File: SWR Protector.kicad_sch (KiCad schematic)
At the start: 27 parts, among them J1 Barrel_Jack, J2 Barrel_Jack, J3 transceiver, J4 antenna, K2 ATX209, Q1 2N3904, T1 1:12, T2 1:12, U1 LM78L05_TO92, U2 LM358

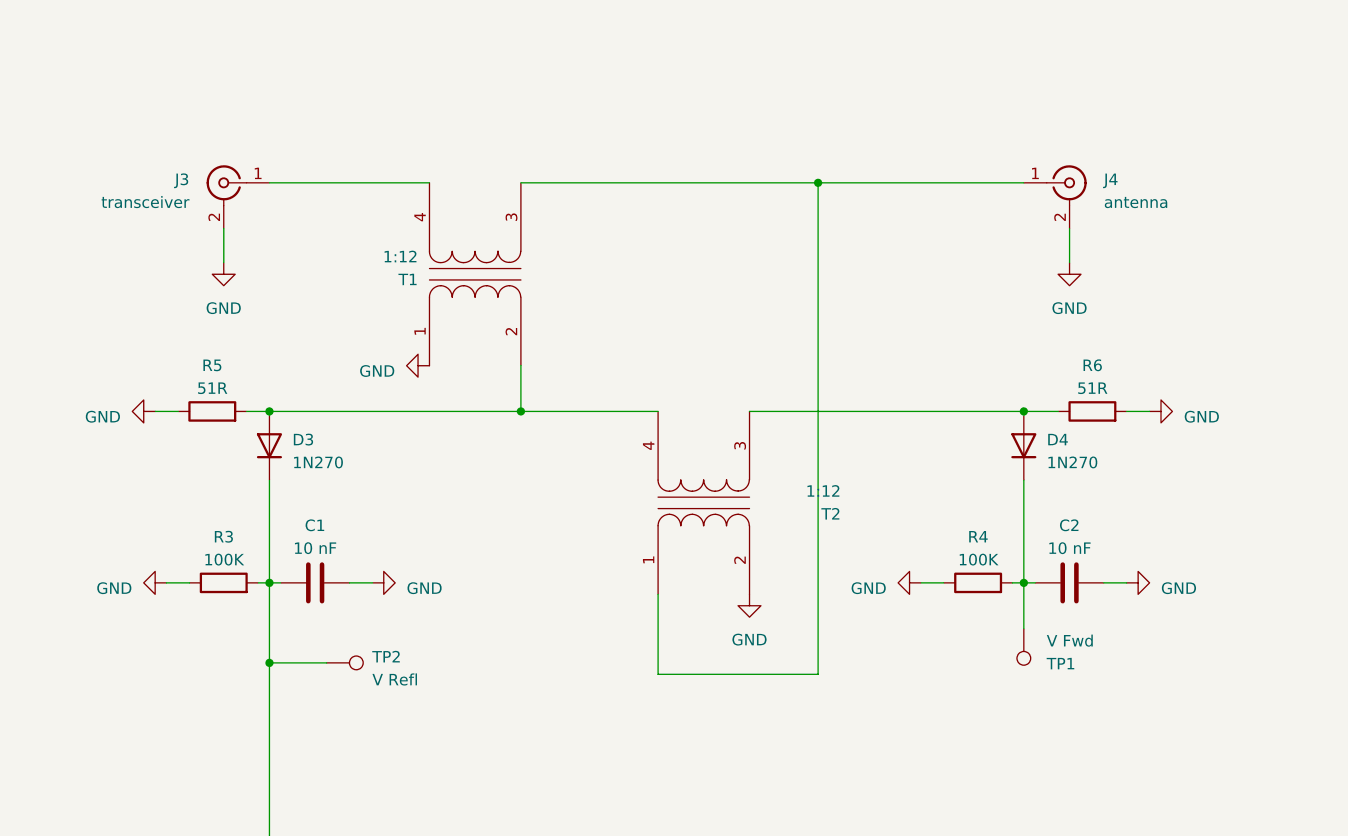
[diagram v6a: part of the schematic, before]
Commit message: moved transceiver BNC jack to the same side of the board as the switched pwr
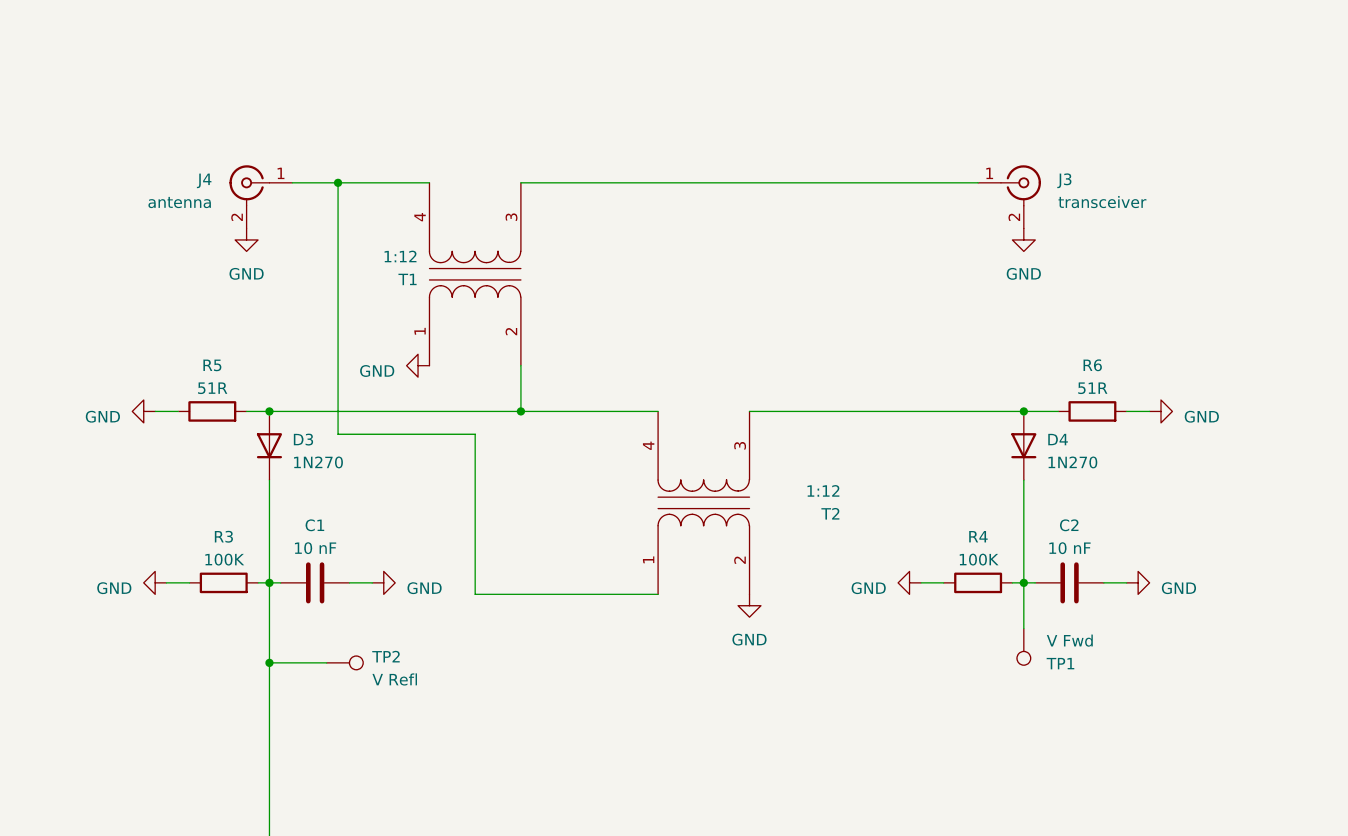
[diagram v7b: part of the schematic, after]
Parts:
- J1, J2: footprint Connector_BarrelJack:BarrelJack_Horizontal -> Connector_BarrelJack:BarrelJack_CUI_PJ-063AH_Horizontal
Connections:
- net at J4.1 (In), T2.1 (AA): now also T1.4 (SB); no longer T1.3 (SA)
- net at J3.1 (In): now also T1.3 (SA); no longer T1.4 (SB)
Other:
- moved on the sheet: J3, J4
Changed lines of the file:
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@@
     (rev "0.6")
   )
-  (junction (at 111.76 35.56) (diameter 0) (color 0 0 0 0)
-  )
   (junction (at 181.61 138.43) (diameter 0) (color 0 0 0 0)
   )
@@
   )
   (junction (at 134.62 60.96) (diameter 0) (color 0 0 0 0)
+  )
+  (junction (at 58.42 35.56) (diameter 0) (color 0 0 0 0)
   )
   (junction (at 240.03 29.21) (diameter 0) (color 0 0 0 0)
@@
     (stroke (width 0) (type default))
   )
+  (wire (pts (xy 58.42 63.5) (xy 58.42 35.56))
+    (stroke (width 0) (type default))
+  )
   (wire (pts (xy 134.62 80.01) (xy 135.89 80.01))
     (stroke (width 0) (type default))
@@
     (stroke (width 0) (type default))
   )
-  (wire (pts (xy 93.98 90.17) (xy 93.98 81.28))
+  (wire (pts (xy 73.66 63.5) (xy 58.42 63.5))
+    (stroke (width 0) (type default))
+  )
+  (wire (pts (xy 53.34 35.56) (xy 58.42 35.56))
     (stroke (width 0) (type default))
   )
@@
     (stroke (width 0) (type default))
   )
-  (wire (pts (xy 78.74 35.56) (xy 111.76 35.56))
-    (stroke (width 0) (type default))
-  )
   (wire (pts (xy 190.5 114.3) (xy 193.04 114.3))
     (stroke (width 0) (type default))
@@
     (stroke (width 0) (type default))
   )
-  (wire (pts (xy 111.76 90.17) (xy 93.98 90.17))
-    (stroke (width 0) (type default))
-  )
   (wire (pts (xy 50.8 60.96) (xy 78.74 60.96))
     (stroke (width 0) (type default))
   )
-  (wire (pts (xy 139.7 40.64) (xy 139.7 44.45))
+  (wire (pts (xy 58.42 35.56) (xy 68.58 35.56))
     (stroke (width 0) (type default))
   )
@@
     (stroke (width 0) (type default))
   )
-  (wire (pts (xy 45.72 40.64) (xy 45.72 44.45))
-    (stroke (width 0) (type default))
-  )
   (wire (pts (xy 181.61 138.43) (xy 181.61 143.51))
     (stroke (width 0) (type default))
@@
     (stroke (width 0) (type default))
   )
+  (wire (pts (xy 93.98 81.28) (xy 73.66 81.28))
+    (stroke (width 0) (type default))
+  )
   (wire (pts (xy 125.73 146.05) (xy 129.54 146.05))
     (stroke (width 0) (type default))
@@
     (stroke (width 0) (type default))
   )
-  (wire (pts (xy 111.76 35.56) (xy 111.76 90.17))
-    (stroke (width 0) (type default))
-  )
   (wire (pts (xy 168.91 138.43) (xy 181.61 138.43))
     (stroke (width 0) (type default))
   )
-  (wire (pts (xy 50.8 35.56) (xy 68.58 35.56))
-    (stroke (width 0) (type default))
-  )
   (wire (pts (xy 133.35 80.01) (xy 134.62 80.01))
     (stroke (width 0) (type default))
@@
     (stroke (width 0) (type default))
   )
+  (wire (pts (xy 73.66 81.28) (xy 73.66 63.5))
+    (stroke (width 0) (type default))
+  )
   (wire (pts (xy 50.8 88.9) (xy 57.15 88.9))
     (stroke (width 0) (type default))
@@
     (stroke (width 0) (type default))
   )
+  (wire (pts (xy 78.74 35.56) (xy 129.54 35.56))
+    (stroke (width 0) (type default))
+  )
   (wire (pts (xy 144.78 143.51) (xy 148.59 143.51))
     (stroke (width 0) (type default))
@@
   )
   (wire (pts (xy 240.03 29.21) (xy 242.57 29.21))
-    (stroke (width 0) (type default))
-  )
-  (wire (pts (xy 111.76 35.56) (xy 134.62 35.56))
     (stroke (width 0) (type default))
   )
@@
     )
   )
-  (symbol (lib_id "power:GND") (at 139.7 44.45 0) (unit 1)
-    (in_bom yes) (on_board yes) (dnp no) (fields_autoplaced)
-    (property "Reference" "#PWR012" (at 139.7 50.8 0)
-      (effects (font (size 1.27 1.27)) hide)
-    )
-    (property "Value" "GND" (at 139.7 49.53 0)
-      (effects (font (size 1.27 1.27)))
-    )
-    (property "Footprint" "" (at 139.7 44.45 0)
-      (effects (font (size 1.27 1.27)) hide)
-    )
-    (property "Datasheet" "" (at 139.7 44.45 0)
+  (symbol (lib_id "power:GND") (at 48.26 40.64 0) (unit 1)
+    (in_bom yes) (on_board yes) (dnp no) (fields_autoplaced)
+    (property "Reference" "#PWR012" (at 48.26 46.99 0)
+      (effects (font (size 1.27 1.27)) hide)
+    )
+    (property "Value" "GND" (at 48.26 45.72 0)
+      (effects (font (size 1.27 1.27)))
+    )
+    (property "Footprint" "" (at 48.26 40.64 0)
+      (effects (font (size 1.27 1.27)) hide)
+    )
+    (property "Datasheet" "" (at 48.26 40.64 0)
       (effects (font (size 1.27 1.27)) hide)
     )
@@
       (effects (font (size 1.27 1.27)))
     )
-    (property "Footprint" "Connector_BarrelJack:BarrelJack_Horizontal" (at 38.1 177.546 0)
+    (property "Footprint" "Connector_BarrelJack:BarrelJack_CUI_PJ-063AH_Horizontal" (at 38.1 177.546 0)
       (effects (font (size 1.27 1.27)) hide)
     )
@@
     )
   )
-  (symbol (lib_id "Connector:Conn_Coaxial") (at 45.72 35.56 0) (mirror y) (unit 1)
-    (in_bom yes) (on_board yes) (dnp no)
-    (property "Reference" "J3" (at 41.91 35.2182 0)
-      (effects (font (size 1.27 1.27)) (justify left))
-    )
-    (property "Value" "transceiver" (at 41.91 37.7582 0)
-      (effects (font (size 1.27 1.27)) (justify left))
-    )
-    (property "Footprint" "Connector_Coaxial:BNC_TEConnectivity_1478035_Horizontal" (at 45.72 35.56 0)
-      (effects (font (size 1.27 1.27)) hide)
-    )
-    (property "Datasheet" " ~" (at 45.72 35.56 0)
+  (symbol (lib_id "Connector:Conn_Coaxial") (at 134.62 35.56 0) (unit 1)
+    (in_bom yes) (on_board yes) (dnp no)
+    (property "Reference" "J3" (at 138.43 35.2182 0)
+      (effects (font (size 1.27 1.27)) (justify left))
+    )
+    (property "Value" "transceiver" (at 138.43 37.7582 0)
+      (effects (font (size 1.27 1.27)) (justify left))
+    )
+    (property "Footprint" "Connector_Coaxial:BNC_TEConnectivity_1478035_Horizontal" (at 134.62 35.56 0)
+      (effects (font (size 1.27 1.27)) hide)
+    )
+    (property "Datasheet" " ~" (at 134.62 35.56 0)
       (effects (font (size 1.27 1.27)) hide)
     )
@@
       (effects (font (size 1.27 1.27)))
     )
-    (property "Footprint" "Connector_BarrelJack:BarrelJack_Horizontal" (at 242.57 144.526 0)
+    (property "Footprint" "Connector_BarrelJack:BarrelJack_CUI_PJ-063AH_Horizontal" (at 242.57 144.526 0)
       (effects (font (size 1.27 1.27)) hide)
     )
@@
     )
   )
-  (symbol (lib_id "Connector:Conn_Coaxial") (at 139.7 35.56 0) (unit 1)
-    (in_bom yes) (on_board yes) (dnp no) (fields_autoplaced)
-    (property "Reference" "J4" (at 143.51 35.2182 0)
-      (effects (font (size 1.27 1.27)) (justify left))
-    )
-    (property "Value" "antenna" (at 143.51 37.7582 0)
-      (effects (font (size 1.27 1.27)) (justify left))
-    )
-    (property "Footprint" "Connector_Coaxial:BNC_TEConnectivity_1478035_Horizontal" (at 139.7 35.56 0)
-      (effects (font (size 1.27 1.27)) hide)
-    )
-    (property "Datasheet" " ~" (at 139.7 35.56 0)
+  (symbol (lib_id "Connector:Conn_Coaxial") (at 48.26 35.56 0) (mirror y) (unit 1)
+    (in_bom yes) (on_board yes) (dnp no)
+    (property "Reference" "J4" (at 44.45 35.2182 0)
+      (effects (font (size 1.27 1.27)) (justify left))
+    )
+    (property "Value" "antenna" (at 44.45 37.7582 0)
+      (effects (font (size 1.27 1.27)) (justify left))
+    )
+    (property "Footprint" "Connector_Coaxial:BNC_TEConnectivity_1478035_Horizontal" (at 48.26 35.56 0)
+      (effects (font (size 1.27 1.27)) hide)
+    )
+    (property "Datasheet" " ~" (at 48.26 35.56 0)
       (effects (font (size 1.27 1.27)) hide)
     )
@@
     )
   )
-  (symbol (lib_id "power:GND") (at 45.72 44.45 0) (unit 1)
-    (in_bom yes) (on_board yes) (dnp no) (fields_autoplaced)
-    (property "Reference" "#PWR010" (at 45.72 50.8 0)
-      (effects (font (size 1.27 1.27)) hide)
-    )
-    (property "Value" "GND" (at 45.72 49.53 0)
-      (effects (font (size 1.27 1.27)))
-    )
-    (property "Footprint" "" (at 45.72 44.45 0)
-      (effects (font (size 1.27 1.27)) hide)
-    )
-    (property "Datasheet" "" (at 45.72 44.45 0)
-      (effects (font (size 1.27 1.27)) hide)
-    )
+  (symbol (lib_id "power:GND") (at 134.62 40.64 0) (unit 1)
+    (in_bom yes) (on_board yes) (dnp no) (fields_autoplaced)
+    (property "Reference" "#PWR010" (at 134.62 46.99 0)
+      (effects (font (size 1.27 1.27)) hide)
+    )
+    (property "Value" "GND" (at 134.62 45.72 0)
+      (effects (font (size 1.27 1.27)))
+    )
+    (property "Footprint" "" (at 134.62 40.64 0)
+      (effects (font (size 1.27 1.27)) hide)
+    )
+    (property "Datasheet" "" (at 134.62 40.64 0)
+      (effects (font (size 1.27 1.27)) hide)
+    )

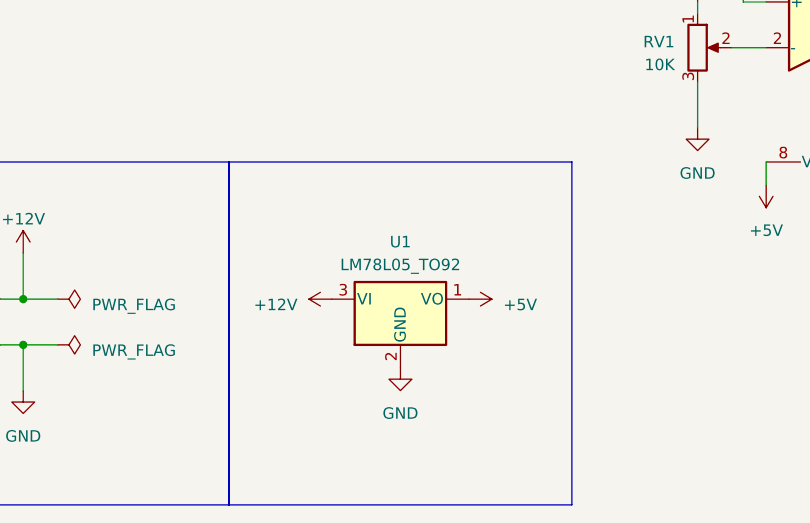
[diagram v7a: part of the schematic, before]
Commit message: Added a couple of caps on the 5V regulator.
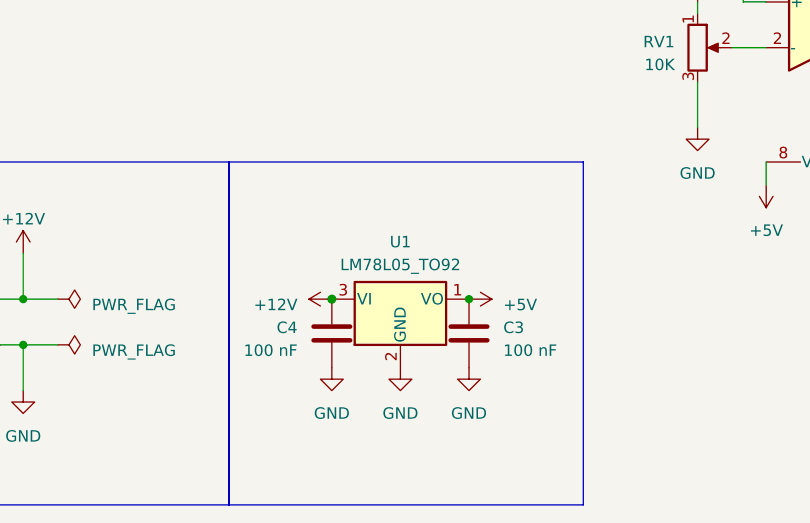
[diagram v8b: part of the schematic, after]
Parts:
- added C3, C4: 100 nF, Capacitor_THT:C_Disc_D5.0mm_W2.5mm_P5.00mm, symbol Device:C
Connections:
- net +12V: now also C4.1
- net +5V: now also C3.1
- net GND: now also C3.2, C4.2
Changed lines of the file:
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@@
   (junction (at 240.03 29.21) (diameter 0) (color 0 0 0 0)
   )
+  (junction (at 96.52 173.99) (diameter 0) (color 0 0 0 0)
+  )
   (junction (at 46.99 179.07) (diameter 0) (color 0 0 0 0)
   )
@@
   )
   (junction (at 46.99 173.99) (diameter 0) (color 0 0 0 0)
+  )
+  (junction (at 81.28 173.99) (diameter 1) (color 0 0 0 0)
   )
   (junction (at 50.8 88.9) (diameter 0) (color 0 0 0 0)
@@
     (stroke (width 0) (type default))
   )
-  (rectangle (start 69.85 158.75) (end 107.95 196.85)
+  (rectangle (start 69.85 158.75) (end 109.22 196.85)
     (stroke (width 0) (type default))
     (fill (type none))
@@
     )
   )
+  (symbol (lib_id "Device:C") (at 81.28 177.8 0) (mirror y) (unit 1)
+    (in_bom yes) (on_board yes) (dnp no)
+    (property "Reference" "C4" (at 77.47 177.165 0)
+      (effects (font (size 1.27 1.27)) (justify left))
+    )
+    (property "Value" "100 nF" (at 77.47 179.705 0)
+      (effects (font (size 1.27 1.27)) (justify left))
+    )
+    (property "Footprint" "Capacitor_THT:C_Disc_D5.0mm_W2.5mm_P5.00mm" (at 80.3148 181.61 0)
+      (effects (font (size 1.27 1.27)) hide)
+    )
+    (property "Datasheet" "~" (at 81.28 177.8 0)
+      (effects (font (size 1.27 1.27)) hide)
+    )
+    (pin "1")
+    (pin "2")
+    (instances
+      (project "SWR Protector"
+        (path "/46027dd5-036f-43c6-98e1-c4cfe473ecd7"
+          (reference "C4") (unit 1)
+        )
+      )
+    )
+  )
   (symbol (lib_id "Connector:Barrel_Jack") (at 243.84 143.51 0) (mirror y) (unit 1)
     (in_bom yes) (on_board yes) (dnp no)
@@
         (path "/46027dd5-036f-43c6-98e1-c4cfe473ecd7"
           (reference "R8") (unit 1)
+        )
+      )
+    )
+  )
+  (symbol (lib_id "power:GND") (at 96.52 181.61 0) (unit 1)
+    (in_bom yes) (on_board yes) (dnp no) (fields_autoplaced)
+    (property "Reference" "#PWR027" (at 96.52 187.96 0)
+      (effects (font (size 1.27 1.27)) hide)
+    )
+    (property "Value" "GND" (at 96.52 186.69 0)
+      (effects (font (size 1.27 1.27)))
+    )
+    (property "Footprint" "" (at 96.52 181.61 0)
+      (effects (font (size 1.27 1.27)) hide)
+    )
+    (property "Datasheet" "" (at 96.52 181.61 0)
+      (effects (font (size 1.27 1.27)) hide)
+    )
+    (pin "1")
+    (instances
+      (project "SWR Protector"
+        (path "/46027dd5-036f-43c6-98e1-c4cfe473ecd7"
+          (reference "#PWR027") (unit 1)
         )
       )
@@
     )
   )
+  (symbol (lib_id "power:GND") (at 81.28 181.61 0) (unit 1)
+    (in_bom yes) (on_board yes) (dnp no) (fields_autoplaced)
+    (property "Reference" "#PWR028" (at 81.28 187.96 0)
+      (effects (font (size 1.27 1.27)) hide)
+    )
+    (property "Value" "GND" (at 81.28 186.69 0)
+      (effects (font (size 1.27 1.27)))
+    )
+    (property "Footprint" "" (at 81.28 181.61 0)
+      (effects (font (size 1.27 1.27)) hide)
+    )
+    (property "Datasheet" "" (at 81.28 181.61 0)
+      (effects (font (size 1.27 1.27)) hide)
+    )
+    (pin "1")
+    (instances
+      (project "SWR Protector"
+        (path "/46027dd5-036f-43c6-98e1-c4cfe473ecd7"
+          (reference "#PWR028") (unit 1)
+        )
+      )
+    )
+  )
   (symbol (lib_id "Device:R") (at 240.03 25.4 0) (mirror y) (unit 1)
     (in_bom yes) (on_board yes) (dnp no)
@@
         )
       )
+    )
+  )
+  (symbol (lib_id "Device:C") (at 96.52 177.8 0) (unit 1)
+    (in_bom yes) (on_board yes) (dnp no) (fields_autoplaced)
+    (property "Reference" "C3" (at 100.33 177.165 0)
+      (effects (font (size 1.27 1.27)) (justify left))
+    )
+    (property "Value" "100 nF" (at 100.33 179.705 0)
+      (effects (font (size 1.27 1.27)) (justify left))
+    )
+    (property "Footprint" "Capacitor_THT:C_Disc_D5.0mm_W2.5mm_P5.00mm" (at 97.4852 181.61 0)
+      (effects (font (size 1.27 1.27)) hide)
+    )
+    (property "Datasheet" "~" (at 96.52 177.8 0)
+      (effects (font (size 1.27 1.27)) hide)
+    )
+    (pin "1")
+    (pin "2")
+    (instances
+      (project "SWR Protector"
+        (path "/46027dd5-036f-43c6-98e1-c4cfe473ecd7"
+          (reference "C3") (unit 1)
+        )
+      )
